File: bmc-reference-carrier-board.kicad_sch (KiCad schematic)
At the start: 0 parts

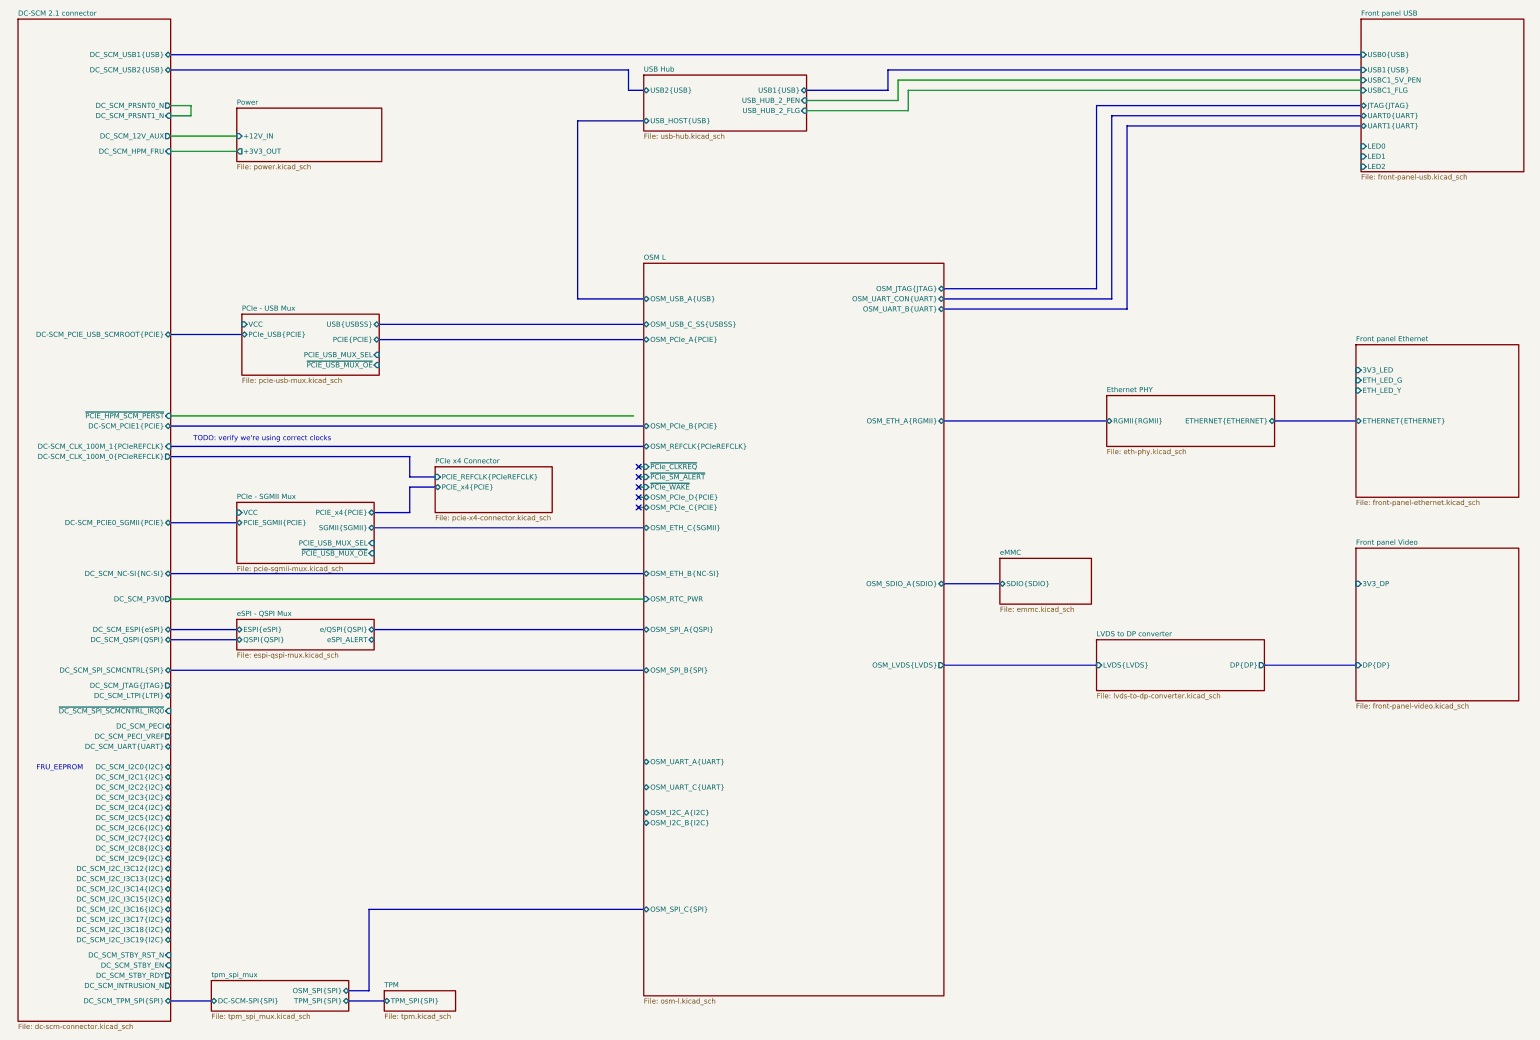
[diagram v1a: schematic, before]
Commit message: [#82323] Connect OSM signals
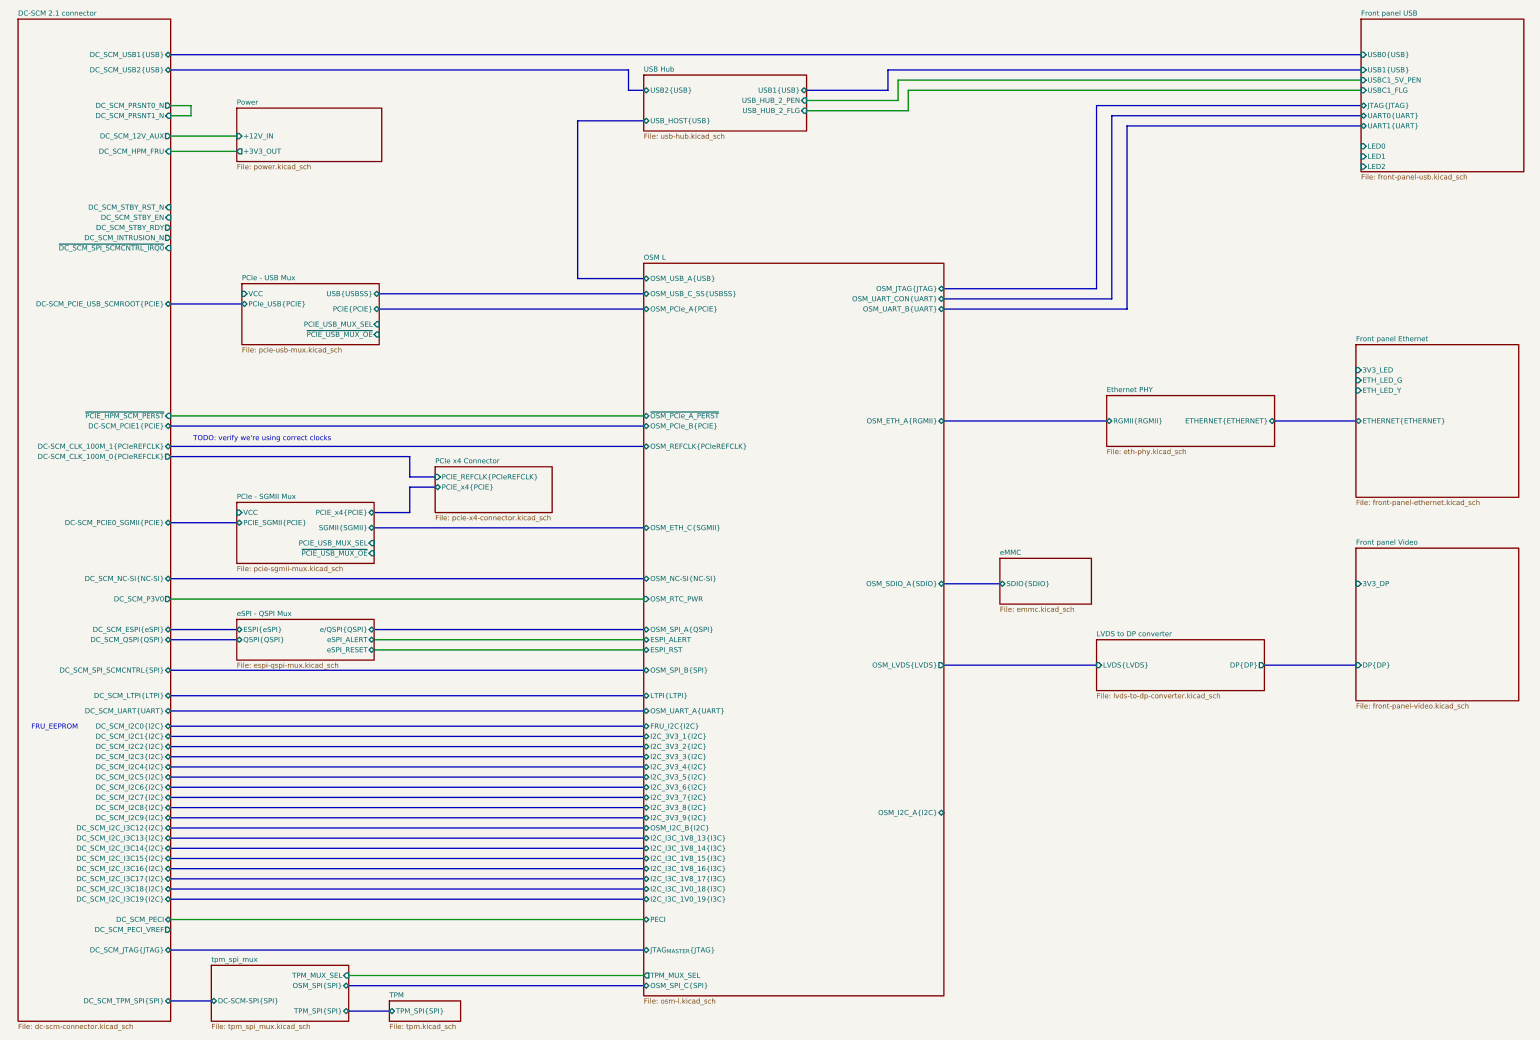
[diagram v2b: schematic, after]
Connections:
- no-connect marks 5 -> 0
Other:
- sheet OSM L ports: added ESPI_ALERT, ESPI_RST, FRU_I2C{I2C}, I2C_3V3_1{I2C}, I2C_3V3_2{I2C}, I2C_3V3_3{I2C}, I2C_3V3_4{I2C}, I2C_3V3_5{I2C}, I2C_3V3_6{I2C}, I2C_3V3_7{I2C}, I2C_3V3_8{I2C}, I2C_3V3_9{I2C}, I2C_I3C_1V0_18{I3C}, I2C_I3C_1V0_19{I3C}, I2C_I3C_1V8_13{I3C}, I2C_I3C_1V8_14{I3C}, I2C_I3C_1V8_15{I3C}, I2C_I3C_1V8_16{I3C}, I2C_I3C_1V8_17{I3C}, JTAG_{MASTER}{JTAG}, LTPI{LTPI}, OSM_NC-SI{NC-SI}, PECI, TPM_MUX_SEL, ~{OSM_PCIe_A_PERST}; removed OSM_ETH_B{NC-SI}, OSM_PCIe_C{PCIE}, OSM_PCIe_D{PCIE}, OSM_UART_C{UART}, ~{PCIe_CLKREQ}, ~{PCIe_SM_ALERT}, ~{PCIe_WAKE}
- sheet eSPI - QSPI Mux ports: added eSPI_RESET; removed none
- sheet tpm_spi_mux ports: added TPM_MUX_SEL; removed none

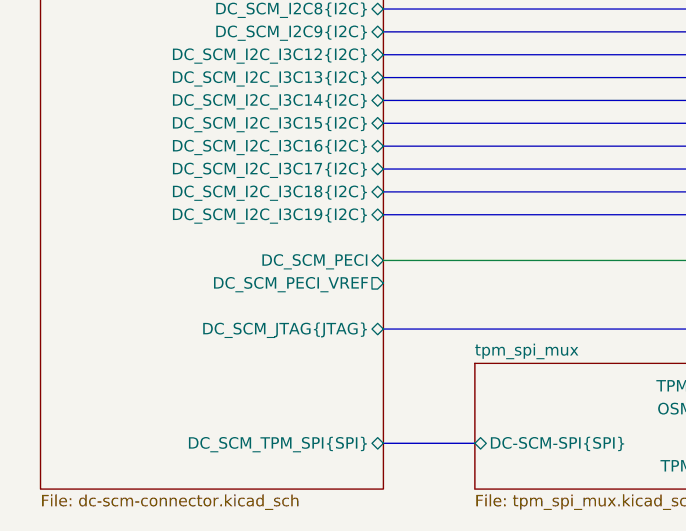
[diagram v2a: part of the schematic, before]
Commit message: [#82323] Add note about PECI voltage translator
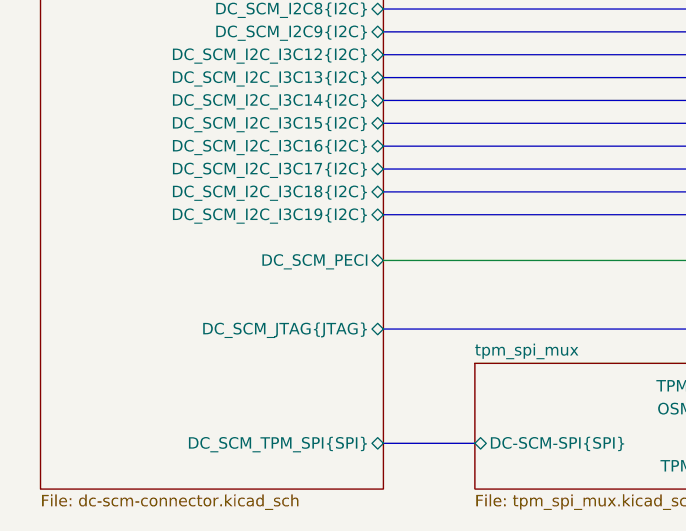
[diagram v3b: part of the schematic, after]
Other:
- sheet DC-SCM 2.1 connector ports: added none; removed DC_SCM_PECI_VREF
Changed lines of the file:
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@@
-			)
-		)
-		(pin "DC_SCM_PECI_VREF" output
-			(at 58.42 252.73 0)
-			(effects
-				(font
-					(size 1.27 1.27)
-				)
-				(justify right)
 			)
 		)

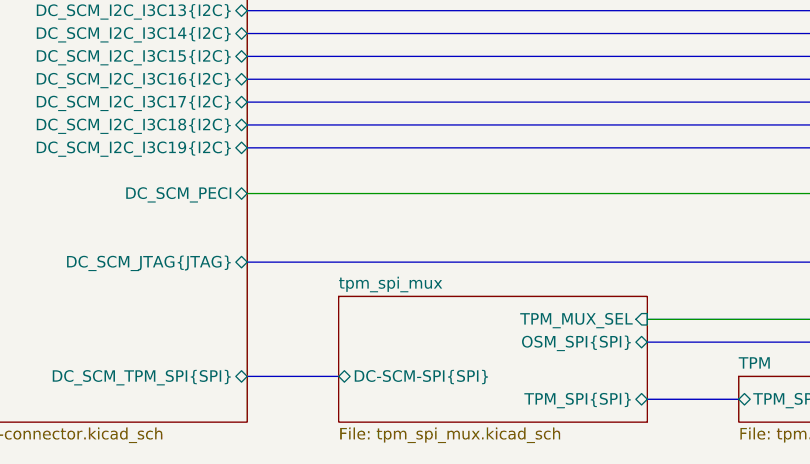
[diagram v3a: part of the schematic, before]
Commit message: [#82323] Update page numbers
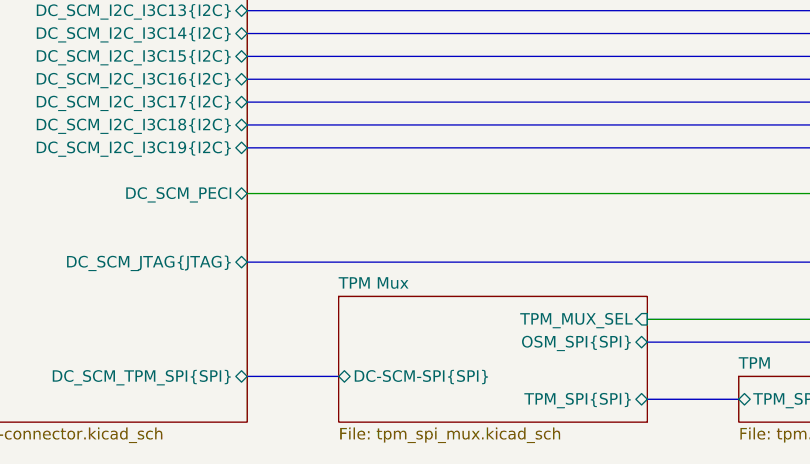
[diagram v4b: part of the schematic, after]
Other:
- sheet tpm_spi_mux renamed TPM Mux
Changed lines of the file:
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@@
 			(project "bmc-reference-carrier-board"
 				(path "/5f636c45-3c15-4731-8931-4625e0dab7e4"
-					(page "10")
+					(page "5")
 				)
 			)
@@
 			(project "bmc-reference-carrier-board"
 				(path "/5f636c45-3c15-4731-8931-4625e0dab7e4"
-					(page "9")
+					(page "4")
 				)
 			)
@@
 			(project "bmc-reference-carrier-board"
 				(path "/5f636c45-3c15-4731-8931-4625e0dab7e4"
-					(page "14")
+					(page "10")
 				)
 			)
@@
 			(project "bmc-reference-carrier-board"
 				(path "/5f636c45-3c15-4731-8931-4625e0dab7e4"
-					(page "17")
+					(page "12")
 				)
 			)
@@
 			(project "bmc-reference-carrier-board"
 				(path "/5f636c45-3c15-4731-8931-4625e0dab7e4"
-					(page "19")
+					(page "17")
 				)
 			)
@@
 			(project "bmc-reference-carrier-board"
 				(path "/5f636c45-3c15-4731-8931-4625e0dab7e4"
-					(page "23")
+					(page "3")
 				)
 			)
@@
 			(project "bmc-reference-carrier-board"
 				(path "/5f636c45-3c15-4731-8931-4625e0dab7e4"
-					(page "11")
+					(page "9")
 				)
 			)
@@
 			(project "bmc-reference-carrier-board"
 				(path "/5f636c45-3c15-4731-8931-4625e0dab7e4"
-					(page "18")
+					(page "13")
 				)
 			)
@@
 			(project "bmc-reference-carrier-board"
 				(path "/5f636c45-3c15-4731-8931-4625e0dab7e4"
-					(page "22")
+					(page "16")
 				)
 			)
@@
 			(project "bmc-reference-carrier-board"
 				(path "/5f636c45-3c15-4731-8931-4625e0dab7e4"
-					(page "15")
+					(page "11")
 				)
 			)
@@
 			(project "bmc-reference-carrier-board"
 				(path "/5f636c45-3c15-4731-8931-4625e0dab7e4"
-					(page "21")
+					(page "15")
 				)
 			)
@@
 			(project "bmc-reference-carrier-board"
 				(path "/5f636c45-3c15-4731-8931-4625e0dab7e4"
-					(page "13")
+					(page "6")
 				)
 			)
@@
 			(color 0 0 0 0.0000)
 		)
-		(property "Sheetname" "tpm_spi_mux"
+		(property "Sheetname" "TPM Mux"
 			(at 68.58 260.9084 0)
 			(effects
@@
 			(project "bmc-reference-carrier-board"
 				(path "/5f636c45-3c15-4731-8931-4625e0dab7e4"
-					(page "18")
+					(page "8")
 				)
 			)
@@
 			(project "bmc-reference-carrier-board"
 				(path "/5f636c45-3c15-4731-8931-4625e0dab7e4"
-					(page "20")
+					(page "14")
 				)
 			)
@@
 			(project "bmc-reference-carrier-board"
 				(path "/5f636c45-3c15-4731-8931-4625e0dab7e4"
-					(page "12")
-				)
-			)
+					(page "7")
+				)
+			)

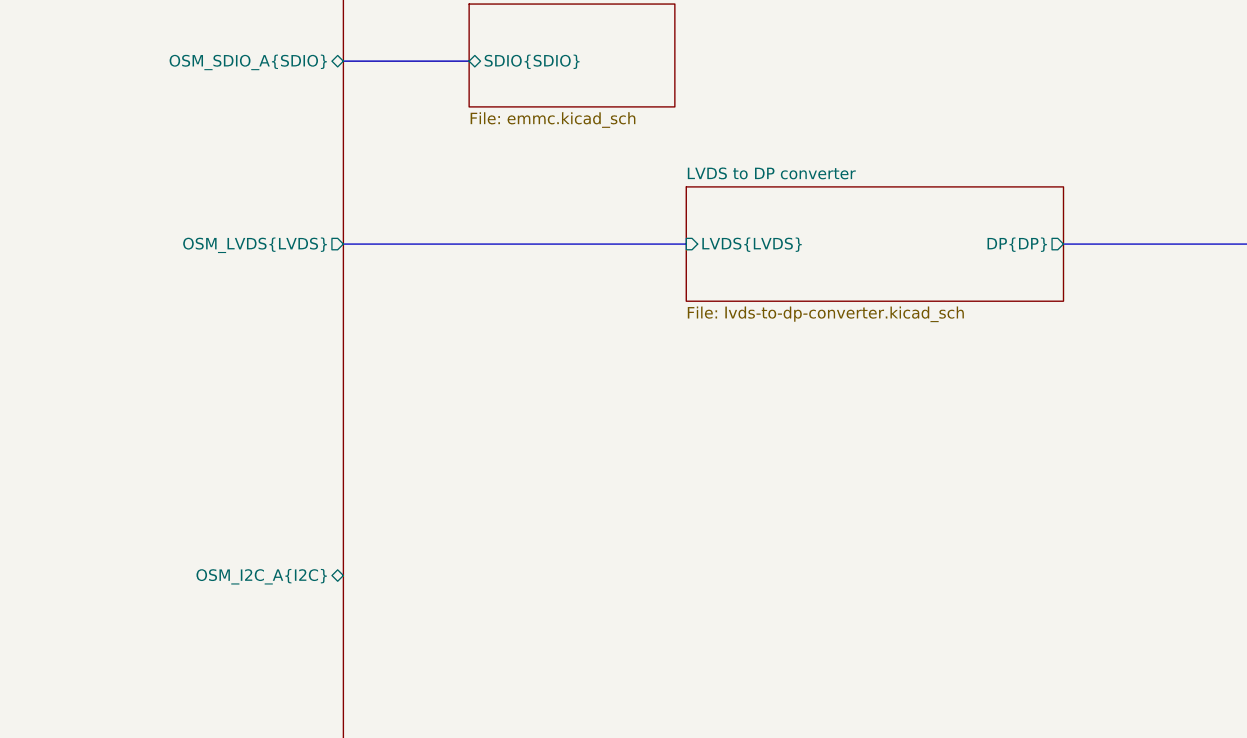
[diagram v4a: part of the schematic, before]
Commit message: [#82341] LVDS/DP Bridge: Connect to OSM
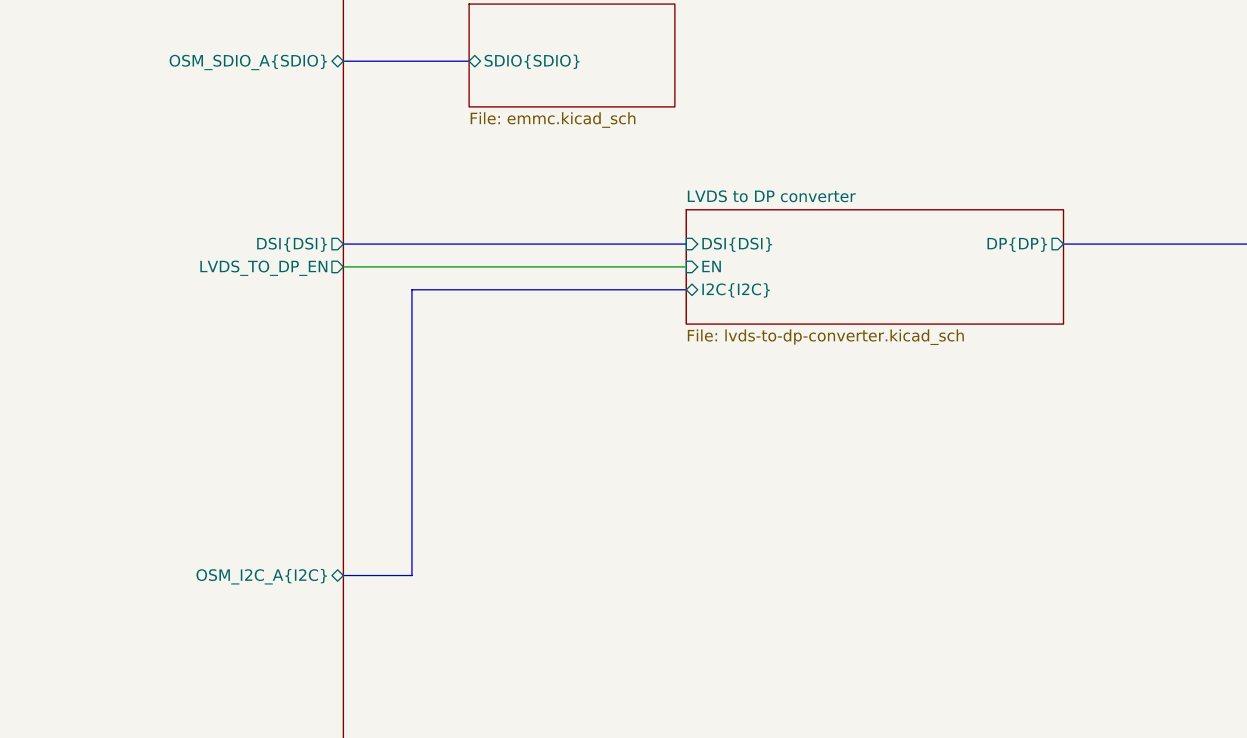
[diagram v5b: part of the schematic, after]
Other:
- sheet LVDS to DP converter ports: added DSI{DSI}, EN, I2C{I2C}; removed LVDS{LVDS}
- sheet OSM L ports: added DSI{DSI}, LVDS_TO_DP_EN; removed OSM_LVDS{LVDS}
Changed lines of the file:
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@@
+	(bus
+		(pts
+			(xy 259.08 191.77) (xy 259.08 223.52)
+		)
+		(stroke
+			(width 0)
+			(type default)
+		)
+	)
 	(bus
 		(pts
@@
 	(bus
 		(pts
+			(xy 259.08 223.52) (xy 251.46 223.52)
+		)
+		(stroke
+			(width 0)
+			(type default)
+		)
+	)
+	(bus
+		(pts
 			(xy 172.72 43.18) (xy 176.53 43.18)
 		)
@@
 		)
 	)
+	(bus
+		(pts
+			(xy 251.46 186.69) (xy 289.56 186.69)
+		)
+		(stroke
+			(width 0)
+			(type default)
+		)
+	)
 	(wire
 		(pts
@@
 	(bus
 		(pts
-			(xy 251.46 186.69) (xy 289.56 186.69)
-		)
-		(stroke
-			(width 0)
-			(type default)
-		)
-	)
-	(bus
-		(pts
 			(xy 109.22 177.8) (xy 176.53 177.8)
 		)
@@
 	(bus
 		(pts
+			(xy 289.56 191.77) (xy 259.08 191.77)
+		)
+		(stroke
+			(width 0)
+			(type default)
+		)
+	)
+	(bus
+		(pts
 			(xy 110.49 97.79) (xy 176.53 97.79)
 		)
@@
 		(pts
 			(xy 63.5 46.99) (xy 63.5 49.53)
+		)
+		(stroke
+			(width 0)
+			(type default)
+		)
+	)
+	(wire
+		(pts
+			(xy 251.46 189.23) (xy 289.56 189.23)
 		)
 		(stroke
@@
 			)
 		)
-		(pin "OSM_LVDS{LVDS}" output
-			(at 251.46 186.69 0)
-			(effects
-				(font
-					(size 1.27 1.27)
-				)
-				(justify right)
-			)
-		)
 		(pin "ESPI_ALERT" bidirectional
 			(at 176.53 180.34 180)
@@
 				)
 				(justify left)
+			)
+		)
+		(pin "DSI{DSI}" output
+			(at 251.46 186.69 0)
+			(effects
+				(font
+					(size 1.27 1.27)
+				)
+				(justify right)
+			)
+		)
+		(pin "LVDS_TO_DP_EN" output
+			(at 251.46 189.23 0)
+			(effects
+				(font
+					(size 1.27 1.27)
+				)
+				(justify right)
 			)
 		)
@@
 	)
 	(sheet
-		(at 289.56 180.34)
+		(at 289.56 182.88)
 		(size 41.91 12.7)
 		(exclude_from_sim no)
@@
 		)
 		(property "Sheetname" "LVDS to DP converter"
-			(at 289.56 179.6284 0)
+			(at 289.56 182.1684 0)
 			(effects
 				(font
@@
 		)
 		(property "Sheetfile" "lvds-to-dp-converter.kicad_sch"
-			(at 289.56 193.6246 0)
+			(at 289.56 196.1646 0)
 			(effects
 				(font
@@
 			)
 		)
-		(pin "LVDS{LVDS}" input
+		(pin "DSI{DSI}" input
 			(at 289.56 186.69 180)
 			(effects
 				(font
+					(size 1.27 1.27)
+				)
+				(justify left)
+			)
+		)
+		(pin "EN" input
+			(at 289.56 189.23 180)
+			(effects
+				(font
+					(size 1.27 1.27)
+				)
+				(justify left)
+			)
+		)
+		(pin "I2C{I2C}" bidirectional
+			(at 289.56 191.77 180)
+			(effects
+				(font
